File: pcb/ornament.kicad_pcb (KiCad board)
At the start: 2 copper layers, 83.4 x 83.4 mm, 14 parts, among them J1 ICSP, U1 ATTINY2313-20MU

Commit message: Add silkscreen.
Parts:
- moved REF** 0.31 mm to (69.8, 28.4)
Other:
- board text added: "2017"
- board text added: "David Tomaschik (@Matir)"
- board text added: "Merry Christmas"
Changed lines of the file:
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@@
     (links 35)
     (no_connects 0)
-    (area 28.103286 23.2222 131.665197 108.828114)
+    (area 28.103286 23.273 131.665197 108.828114)
     (thickness 1.6)
-    (drawings 2)
+    (drawings 5)
     (tracks 137)
     (zones 0)
@@
     (mod_text_size 1 1)
     (mod_text_width 0.15)
-    (pad_size 1.25 1.25)
+    (pad_size 17.780001 17.780001)
     (pad_drill 0)
     (pad_to_mask_clearance 0.2)
@@
     (visible_elements FFFFFF7F)
     (pcbplotparams
-      (layerselection 0x010d0_80000001)
+      (layerselection 0x010f0_80000001)
       (usegerberextensions true)
       (excludeedgelayer true)
@@
   )
   (module Mounting_Holes:MountingHole_3.2mm_M3 (layer F.Cu)
-    (at 69.5452 28.3972)
+    (at 69.85 28.448)
     (descr "Mounting Hole 3.2mm, no annular, M3")
     (tags "mounting hole 3.2mm no annular m3")
@@
   (module footprints:BAT_HLD (layer B.Cu)
     (at 69.977 63.5)
-    (fp_text reference BT1 (at 0 0) (layer B.SilkS)
-      (effects (font (size 1 1) (thickness 0.15)) (justify mirror))
-    )
-    (fp_text value Battery_Cell (at 0 0) (layer B.SilkS)
+    (fp_text reference BT1 (at 0 0) (layer B.SilkS) hide
+      (effects (font (size 1 1) (thickness 0.15)) (justify mirror))
+    )
+    (fp_text value Battery_Cell (at 0 0) (layer B.SilkS) hide
       (effects (font (size 1 1) (thickness 0.15)) (justify mirror))
     )
@@
       (net 1 VCC))
     (pad 2 smd circle (at 0 0) (size 17.780001 17.780001) (layers B.Cu B.Mask)
-      (net 2 GND))
+      (net 2 GND) (thermal_width 3) (thermal_gap 0.4))
+  )
+  (gr_text "David Tomaschik\n(@Matir)" (at 69.596 92.202) (layer B.SilkS)
+    (effects (font (size 2 2) (thickness 0.4)) (justify mirror))
+  )
+  (gr_text 2017 (at 70.104 46.355) (layer B.SilkS)
+    (effects (font (size 6 6) (thickness 1.2)) (justify mirror))
+  )
+  (gr_text "Merry Christmas" (at 69.596 38.735) (layer B.SilkS)
+    (effects (font (size 3 3) (thickness 0.6)) (justify mirror))
   )
   (dimension 83.312387 (width 0.3) (layer Dwgs.User)

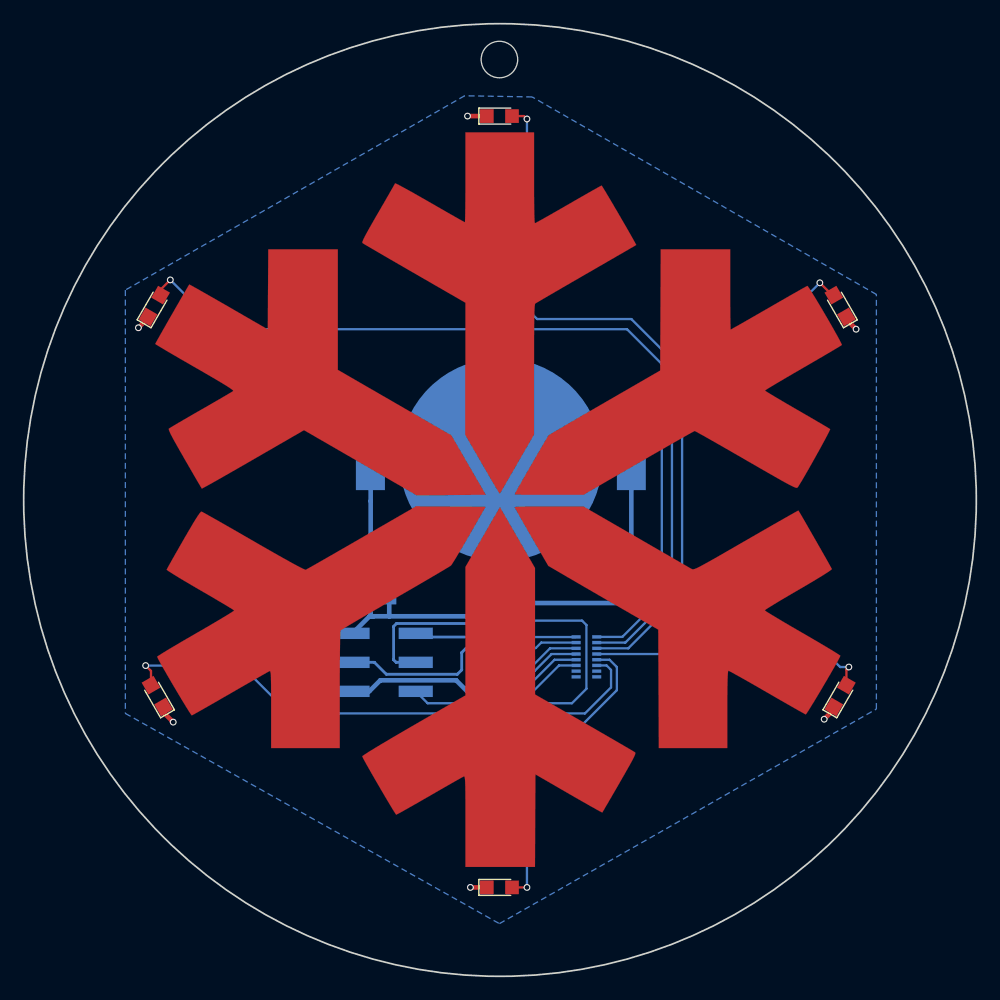
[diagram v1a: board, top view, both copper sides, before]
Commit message: Thicker traces.
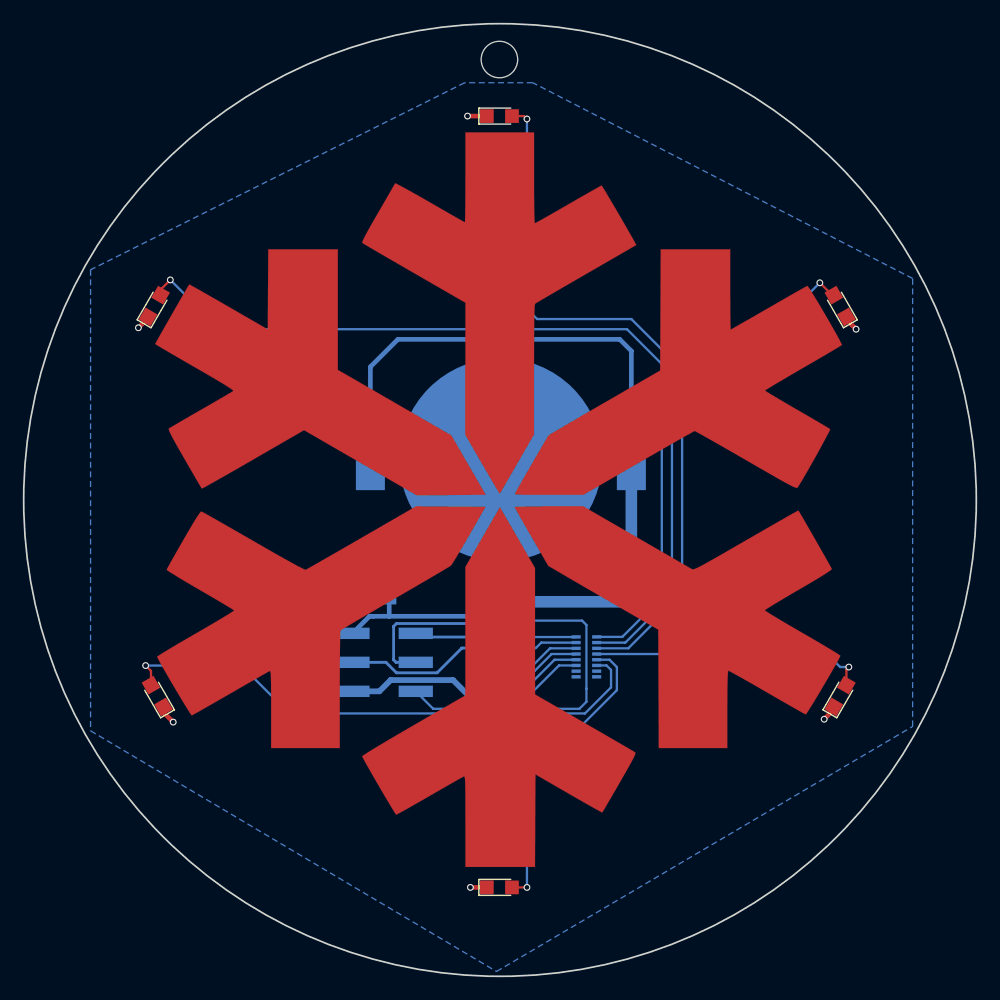
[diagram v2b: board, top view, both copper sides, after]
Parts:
- moved C1 1.55 mm to (68.8, 75.9), turned to 180 degrees
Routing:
- net VCC: track 56.0 -> 113.1 mm
- net GND: track 25.8 -> 28.5 mm
- net /~RESET: track 29.8 -> 30.8 mm
- net /MOSI: track 13.3 -> 12.3 mm
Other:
- net class Default: clearance 0.2 -> 0.1778; trace_width 0.25 -> 0.2032
- rule trace_clearance: 0.2 -> 0.1778
